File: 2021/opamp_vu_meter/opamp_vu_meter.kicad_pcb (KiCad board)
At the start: 2 copper layers, 80 x 100 mm, 44 parts, among them J1 Conn_01x02, J2 Conn_01x02, Q1 Q_PNP_BCE, U1 TLC272, U2 TLC272, U3 TLC272, U4 TLC272, U5 TLC272

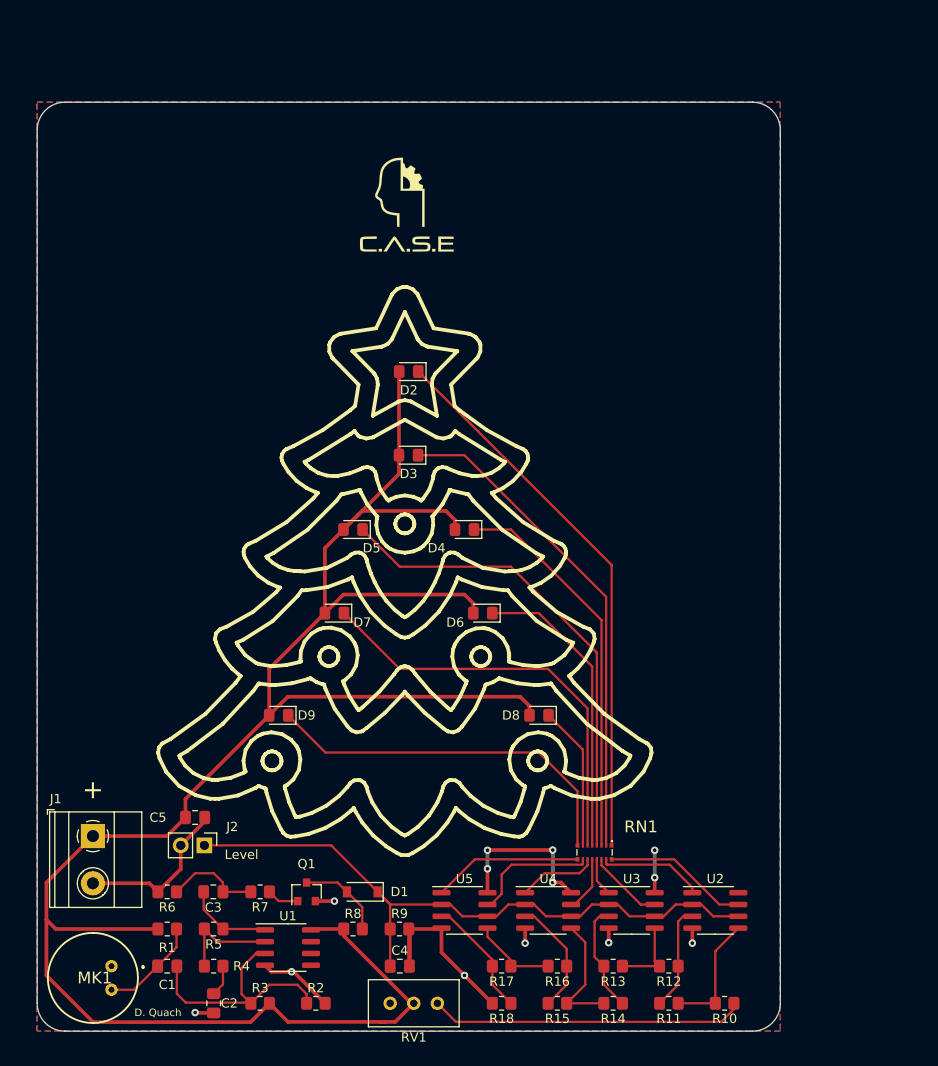
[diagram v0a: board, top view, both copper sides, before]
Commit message: Changed outline shape and component placement
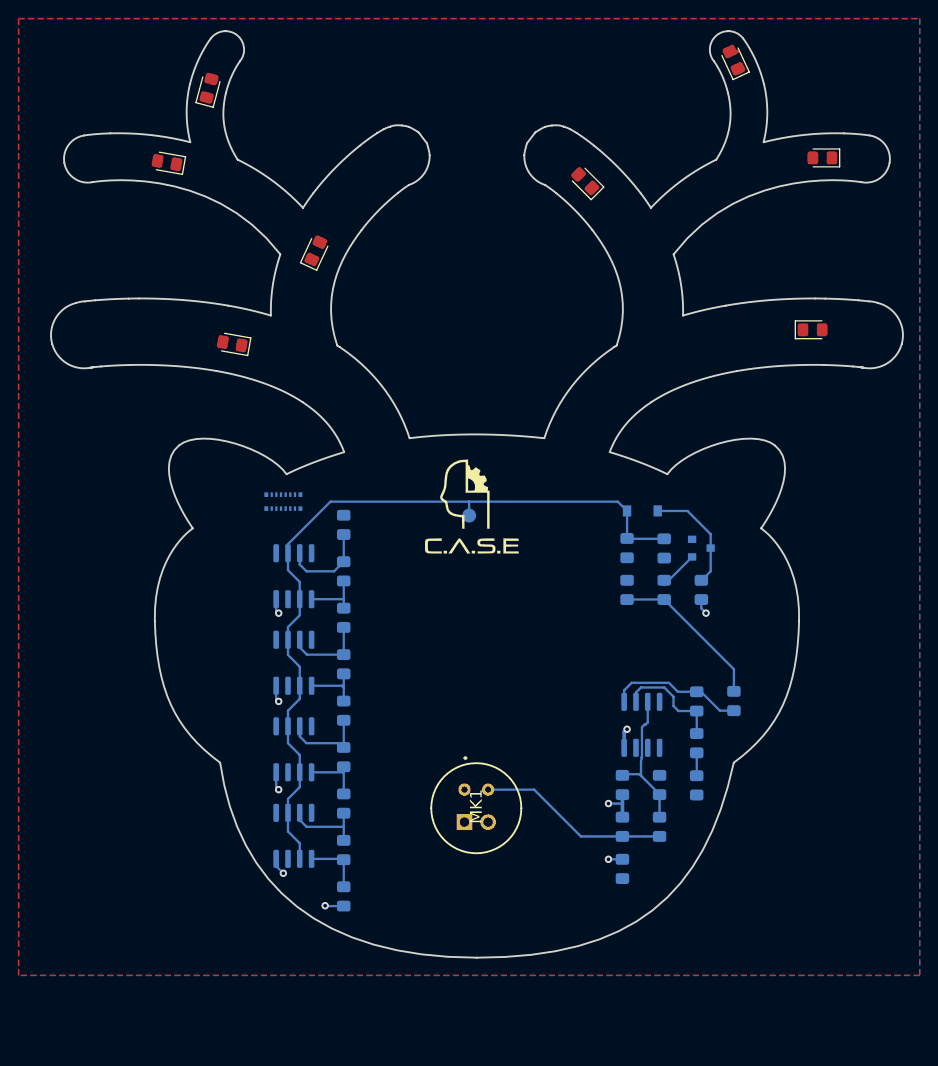
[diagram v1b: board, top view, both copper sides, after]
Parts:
- removed J2: Conn_01x02, Connector_PinHeader_2.54mm:PinHeader_1x02_P2.54mm_Vertical
- removed RV1: R_POT, Potentiometer_THT:Potentiometer_Bourns_3296W_Vertical
- added TP1: TestPoint, TestPoint:TestPoint_Pad_D1.5mm, B.Cu at (149.5, 83.5)
- C1, C2, C3, C4, C5: footprint Capacitor_SMD:C_0805_2012Metric_Pad1.18x1.45mm_HandSolder -> opamp_vu_meter:C_0805_2012Metric_Pad1.18x1.45mm_HandSolder_silkVal; moved to B.Cu
- D1, Q1, RN1, U1, U2, U3, U4, U5: moved to B.Cu
- J1: footprint TerminalBlock_Phoenix:TerminalBlock_Phoenix_MKDS-1,5-2-5.08_1x02_P5.08mm_Horizontal -> Connector_PinHeader_2.54mm:PinHeader_1x02_P2.54mm_Vertical; moved to B.Cu
- R1, R2, R3, R6, R7, R8, R9: footprint Resistor_SMD:R_0805_2012Metric_Pad1.20x1.40mm_HandSolder -> opamp_vu_meter:C_0805_2012Metric_Pad1.18x1.45mm_HandSolder_silkVal; moved to B.Cu
- R10, R18: value R_Small -> 43k; footprint Resistor_SMD:R_0805_2012Metric_Pad1.20x1.40mm_HandSolder -> opamp_vu_meter:C_0805_2012Metric_Pad1.18x1.45mm_HandSolder_silkVal; moved to B.Cu
- R11: value R_Small -> 6.2k; footprint Resistor_SMD:R_0805_2012Metric_Pad1.20x1.40mm_HandSolder -> opamp_vu_meter:C_0805_2012Metric_Pad1.18x1.45mm_HandSolder_silkVal; moved to B.Cu
- R12: value R_Small -> 4.3k; footprint Resistor_SMD:R_0805_2012Metric_Pad1.20x1.40mm_HandSolder -> opamp_vu_meter:C_0805_2012Metric_Pad1.18x1.45mm_HandSolder_silkVal; moved to B.Cu
- R13: value R_Small -> 3k; footprint Resistor_SMD:R_0805_2012Metric_Pad1.20x1.40mm_HandSolder -> opamp_vu_meter:C_0805_2012Metric_Pad1.18x1.45mm_HandSolder_silkVal; moved to B.Cu
- R14: value R_Small -> 2.2k; footprint Resistor_SMD:R_0805_2012Metric_Pad1.20x1.40mm_HandSolder -> opamp_vu_meter:C_0805_2012Metric_Pad1.18x1.45mm_HandSolder_silkVal; moved to B.Cu
- R15: value R_Small -> 1.6k; footprint Resistor_SMD:R_0805_2012Metric_Pad1.20x1.40mm_HandSolder -> opamp_vu_meter:C_0805_2012Metric_Pad1.18x1.45mm_HandSolder_silkVal; moved to B.Cu
- R16: value R_Small -> 1.1k; footprint Resistor_SMD:R_0805_2012Metric_Pad1.20x1.40mm_HandSolder -> opamp_vu_meter:C_0805_2012Metric_Pad1.18x1.45mm_HandSolder_silkVal; moved to B.Cu
- R17: value R_Small -> 750R; footprint Resistor_SMD:R_0805_2012Metric_Pad1.20x1.40mm_HandSolder -> opamp_vu_meter:C_0805_2012Metric_Pad1.18x1.45mm_HandSolder_silkVal; moved to B.Cu
- R4: value 10k -> 1k; footprint Resistor_SMD:R_0805_2012Metric_Pad1.20x1.40mm_HandSolder -> opamp_vu_meter:C_0805_2012Metric_Pad1.18x1.45mm_HandSolder_silkVal; moved to B.Cu
- R5: value 100k -> 200k; footprint Resistor_SMD:R_0805_2012Metric_Pad1.20x1.40mm_HandSolder -> opamp_vu_meter:C_0805_2012Metric_Pad1.18x1.45mm_HandSolder_silkVal; moved to B.Cu
- moved D9 70.9 mm to (186.5, 63.5), turned to 0 degrees
- moved D5 64.4 mm to (187.5, 45.0)
- moved C3 59.7 mm to (178.0, 103.5), turned to 270 degrees
- moved R6 59.2 mm to (166.5, 91.5), turned to 90 degrees
- moved R5 57.5 mm to (174.0, 103.5), turned to 270 degrees
- moved R4 57.3 mm to (174.0, 108.0), turned to 270 degrees
- moved C2 57.0 mm to (174.0, 112.5)
- moved Q1 56.3 mm to (174.5, 87.0), turned to 0 degrees
- moved C1 55.1 mm to (170.0, 117.0), turned to 90 degrees
- moved R7 54.3 mm to (170.5, 91.5), turned to 270 degrees
- moved R18 54.2 mm to (136.0, 84.5), turned to 90 degrees
- moved D7 53.8 mm to (162.0, 47.5), turned to 135 degrees
- moved C4 53.2 mm to (170.5, 87.0), turned to 270 degrees
- moved R8 52.3 mm to (174.5, 91.5), turned to 90 degrees
- moved D8 51.9 mm to (124.0, 65.0), turned to 170 degrees
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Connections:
- J1 pad 1: VCC -> GND
- J1 pad 2: GND -> VCC
- R10 pad 1: Net-(R10-Pad1) -> VCC
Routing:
- net VCC: track 242.2 -> 19.3 mm, vias 6 -> 9
- net Net-(D2-Pad1): track 59.6 -> 0.00 mm
- net Net-(D3-Pad1): track 53.3 -> 0.00 mm
- net GND: track 52.5 -> 0.00 mm, vias 7 -> 0
- net Net-(D5-Pad1): track 51.5 -> 0.00 mm
- net Net-(D7-Pad1): track 45.2 -> 0.00 mm
- net Net-(D4-Pad1): track 42.0 -> 0.00 mm
- net Net-(D9-Pad1): track 40.4 -> 0.00 mm
- net Net-(R10-Pad1): track 33.8 -> 0.00 mm
- net Net-(D6-Pad1): track 32.4 -> 0.00 mm
- net Net-(RN1-Pad9): track 16.1 -> 0.00 mm
- net Net-(RN1-Pad10): track 15.7 -> 0.00 mm
- net Net-(D8-Pad1): track 15.5 -> 0.00 mm
- net Net-(RN1-Pad11): track 13.8 -> 0.00 mm
- net AudioLevel: track 72.4 -> 84.8 mm
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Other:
- board size 80 x 100 mm -> 91.7 x 99.7 mm
- board text added: "AMPLIFIER"
- board text added: "Audio Level"
- board text added: "BATTERY"
- board text added: "JLCJLCJLCJLC"
- board text added: "LOGARITHMIC ADC + LED DRIVER"
- board text added: "PEAK DETECTOR"
- board text removed: "+"
- board text removed: "Level"

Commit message: Final version (hopefully)
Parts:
- removed R10: 43k, opamp_vu_meter:C_0805_2012Metric_Pad1.18x1.45mm_HandSolder_silkVal
- removed TP1: TestPoint, TestPoint:TestPoint_Pad_D1.5mm
- added Audiolevel_TP1: TestPoint, TestPoint:TestPoint_Pad_D1.5mm, B.Cu at (150.0, 89.5)
- added G***: LOGO, print:godjul, F.Cu at (151.0, 78.8)
- added G***: LOGO, print:eyes, F.Cu at (150.5, 101.0)
- added REF**: MountingHole_3.2mm_M3, MountingHole:MountingHole_3.2mm_M3, F.Cu at (122.5, 80.0)
- added REF**: MountingHole_3.2mm_M3, MountingHole:MountingHole_3.2mm_M3, F.Cu at (178.5, 80.0)
- added RN2: R_Pack04, opamp_vu_meter:R_Array_Convex_4x1206_long, B.Cu at (125.0, 94.7)
- added RV1: R_POT, Potentiometer_SMD:Potentiometer_Bourns_TC33X_Vertical, B.Cu at (134.0, 124.0)
- C4: value C_Small -> 220nF
- R5: value 200k -> 100k
- R9: value R_Small -> 220K
- RN1: value EXB-2HV331JV -> R_Pack04; footprint SamacSys_Parts:EXB2HV331JV -> opamp_vu_meter:R_Array_Convex_4x1206_long
- moved RN1 22.7 mm to (125.0, 104.2), turned to 90 degrees
- moved D8 12.8 mm to (111.2, 64.1), turned to 180 degrees
- moved D6 8.59 mm to (138.0, 48.0), turned to 45 degrees
- moved D7 7.65 mm to (166.8, 53.5), turned to 120 degrees
- moved D9 7.23 mm to (179.3, 64.2), turned to 5 degrees
- moved D5 6.10 mm to (181.5, 46.2), turned to 10 degrees
- moved G*** 4.28 mm to (149.5, 86.8)
- moved D3 2.93 mm to (122.5, 34.8), turned to 70 degrees
- moved D2 2.82 mm to (179.2, 37.0), turned to 105 degrees
- moved D4 1.99 mm to (115.0, 45.2), turned to 175 degrees
- moved R11 0.50 mm to (136.5, 119.5)
- moved R12 0.50 mm to (136.5, 114.5)
- moved R13 0.50 mm to (136.5, 109.5)
- moved R14 0.50 mm to (136.5, 104.5)
- moved R15 0.50 mm to (136.5, 99.5)
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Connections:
- RN1 pad 1: Net-(D2-Pad1) -> Net-(RN1-Pad1)
- RN1 pad 2: Net-(D3-Pad1) -> Net-(RN1-Pad2)
- RN1 pad 3: Net-(D4-Pad1) -> Net-(RN1-Pad3)
- RN1 pad 4: Net-(D5-Pad1) -> Net-(RN1-Pad4)
- RN1 pad 5: Net-(D6-Pad1) -> Net-(D5-Pad1)
- RN1 pad 6: Net-(D7-Pad1) -> Net-(D4-Pad1)
- RN1 pad 7: Net-(D8-Pad1) -> Net-(D3-Pad1)
- RN1 pad 8: Net-(D9-Pad1) -> Net-(D2-Pad1)
- U2 pad 1: Net-(RN1-Pad16) -> Net-(RN1-Pad2)
- U2 pad 7: Net-(RN1-Pad10) -> Net-(RN1-Pad1)
- U3 pad 1: Net-(RN1-Pad14) -> Net-(RN1-Pad4)
- U3 pad 7: Net-(RN1-Pad15) -> Net-(RN1-Pad3)
- U4 pad 1: Net-(RN1-Pad12) -> Net-(RN2-Pad2)
- U4 pad 7: Net-(RN1-Pad13) -> Net-(RN2-Pad1)
- U5 pad 1: Net-(RN1-Pad9) -> Net-(RN2-Pad4)
- U5 pad 7: Net-(RN1-Pad11) -> Net-(RN2-Pad3)
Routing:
- net Net-(D2-Pad1): track 0.00 -> 108.6 mm, vias 0 -> 1
- net Net-(D5-Pad1): track 0.00 -> 103.1 mm, vias 0 -> 1
- net Net-(D3-Pad1): track 0.00 -> 85.7 mm, vias 0 -> 1
- net Net-(D4-Pad1): track 0.00 -> 80.6 mm, vias 0 -> 1
- net Net-(D7-Pad1): track 0.00 -> 72.5 mm, vias 0 -> 1
- net Net-(D9-Pad1): track 0.00 -> 72.2 mm, vias 0 -> 1
- net Net-(D6-Pad1): track 0.00 -> 60.2 mm, vias 0 -> 1
- net Net-(D8-Pad1): track 0.00 -> 59.0 mm, vias 0 -> 1
- net Net-(RN1-Pad1): track 0.00 -> 15.9 mm
- net Net-(RN2-Pad4): track 0.00 -> 13.4 mm
- net Net-(RN1-Pad3): track 0.00 -> 12.2 mm
- net Net-(RN1-Pad2): track 0.00 -> 11.0 mm
- net Net-(RN1-Pad4): track 0.00 -> 10.4 mm
- net Net-(RN2-Pad3): track 0.00 -> 9.03 mm
- net Net-(RN2-Pad1): track 0.00 -> 6.77 mm
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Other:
- board text added: "A. Anderson"
- board text added: "CASE julkort 2021"
- board text added: "LOGARITHMIC COMPARATORS"
- board text removed: "Audio Level"
- board text removed: "LOGARITHMIC ADC + LED DRIVER"

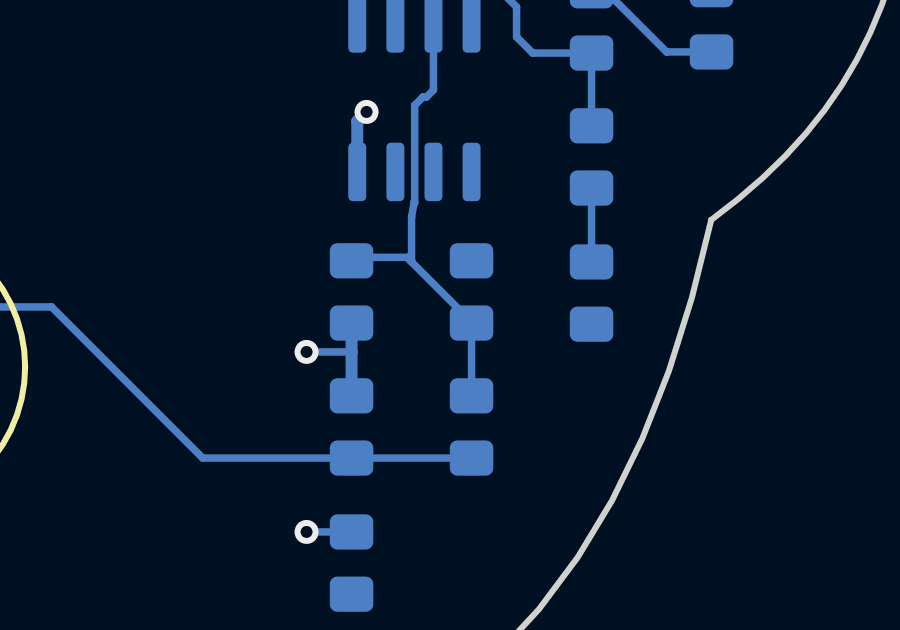
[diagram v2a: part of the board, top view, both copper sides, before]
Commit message: Minor revision with zener to stabilize
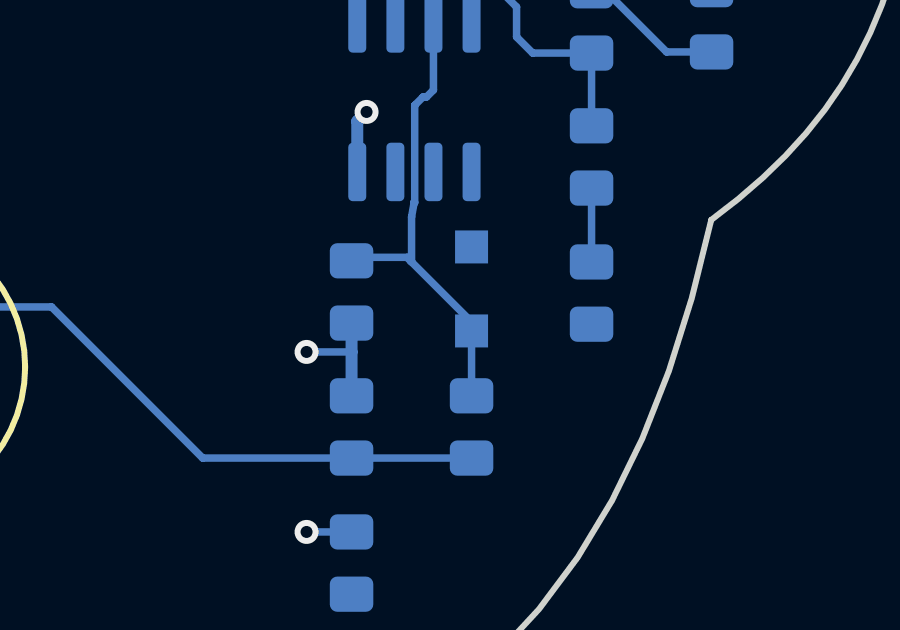
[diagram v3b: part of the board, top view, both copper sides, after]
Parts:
- removed R2: 100k, opamp_vu_meter:C_0805_2012Metric_Pad1.18x1.45mm_HandSolder_silkVal
- added Z1: MM3Z4V3, Diode_SMD:D_SOD-123F, B.Cu at (170.0, 112.4)
- C5: value 1uF -> 10uF
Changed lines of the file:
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@@
       (psa4output false)
       (plotreference true)
-      (plotvalue false)
+      (plotvalue true)
       (plotinvisibletext false)
       (padsonsilk false)
@@
       (effects (font (size 1 1) (thickness 0.15)))
     )
-    (fp_text user %R (at 0.3 0) (layer F.Fab)
-      (effects (font (size 1 1) (thickness 0.15)))
-    )
     (fp_circle (center 0 0) (end 3.2 0) (layer Cmts.User) (width 0.15))
     (fp_circle (center 0 0) (end 3.45 0) (layer F.CrtYd) (width 0.05))
+    (fp_text user %R (at 0.3 0) (layer F.Fab)
+      (effects (font (size 1 1) (thickness 0.15)))
+    )
     (pad 1 np_thru_hole circle (at 0 0) (size 3.2 3.2) (drill 3.2) (layers *.Cu *.Mask))
   )
@@
       (effects (font (size 1 1) (thickness 0.15)))
     )
-    (fp_text value 1uF (at -0.0375 -1.5 90) (layer B.SilkS)
+    (fp_text value 10uF (at -0.0375 -1.5 90) (layer B.SilkS)
       (effects (font (size 1 1) (thickness 0.15)) (justify mirror))
     )
@@
     (pad 1 smd roundrect (at -1.0375 0 90) (size 1.175 1.45) (layers B.Cu B.Paste B.Mask) (roundrect_rratio 0.2127659574468085)
       (net 26 "Net-(R17-Pad2)"))
-    (model ${KISYS3DMOD}/Capacitor_SMD.3dshapes/C_0805_2012Metric.wrl
-      (at (xyz 0 0 0))
-      (scale (xyz 1 1 1))
-      (rotate (xyz 0 0 0))
-    )
-  )
-  (module opamp_vu_meter:C_0805_2012Metric_Pad1.18x1.45mm_HandSolder_silkVal (layer B.Cu)
-    (at 170 112.5 90)
-    (descr "Capacitor SMD 0805 (2012 Metric), square (rectangular) end terminal, IPC_7351 nominal with elongated pad for handsoldering. (Body size source: IPC-SM-782 page 76, https://www.pcb-3d.com/wordpress/wp-content/uploads/ipc-sm-782a_amendment_1_and_2.pdf, https://docs.google.com/spreadsheets/d/1BsfQQcO9C6DZCsRaXUlFlo91Tg2WpOkGARC1WS5S8t0/edit?usp=sharing), generated with kicad-footprint-generator")
-    (tags "capacitor handsolder")
-    (attr smd)
-    (fp_text reference R2 (at -0.0375 -1.5 90) (layer F.Fab) hide
-      (effects (font (size 1 1) (thickness 0.15)))
-    )
-    (fp_text value 100k (at 0 -1.5 90) (layer B.SilkS)
-      (effects (font (size 1 1) (thickness 0.15)) (justify mirror))
-    )
-    (fp_line (start 1.88 -0.98) (end -1.88 -0.98) (layer B.CrtYd) (width 0.05))
-    (fp_line (start 1.88 0.98) (end 1.88 -0.98) (layer B.CrtYd) (width 0.05))
-    (fp_line (start -1.88 0.98) (end 1.88 0.98) (layer B.CrtYd) (width 0.05))
-    (fp_line (start -1.88 -0.98) (end -1.88 0.98) (layer B.CrtYd) (width 0.05))
-    (fp_line (start -0.261252 -0.735) (end 0.261252 -0.735) (layer B.SilkS) (width 0.12))
-    (fp_line (start -0.261252 0.735) (end 0.261252 0.735) (layer B.SilkS) (width 0.12))
-    (fp_line (start 1 -0.625) (end -1 -0.625) (layer B.Fab) (width 0.1))
-    (fp_line (start 1 0.625) (end 1 -0.625) (layer B.Fab) (width 0.1))
-    (fp_line (start -1 0.625) (end 1 0.625) (layer B.Fab) (width 0.1))
-    (fp_line (start -1 -0.625) (end -1 0.625) (layer B.Fab) (width 0.1))
-    (fp_text user %R (at -0.0375 0 90) (layer B.Fab)
-      (effects (font (size 0.5 0.5) (thickness 0.08)) (justify mirror))
-    )
-    (pad 2 smd roundrect (at 1.0375 0 90) (size 1.175 1.45) (layers B.Cu B.Paste B.Mask) (roundrect_rratio 0.2127659574468085)
-      (net 4 GND))
-    (pad 1 smd roundrect (at -1.0375 0 90) (size 1.175 1.45) (layers B.Cu B.Paste B.Mask) (roundrect_rratio 0.2127659574468085)
-      (net 1 "Net-(C1-Pad2)"))
     (model ${KISYS3DMOD}/Capacitor_SMD.3dshapes/C_0805_2012Metric.wrl
       (at (xyz 0 0 0))
@@
     (pad 1 smd circle (at 0 0) (size 1.5 1.5) (layers B.Cu B.Mask)
       (net 7 AudioLevel))
+  )
+  (module Diode_SMD:D_SOD-123F (layer B.Cu)
+    (at 170 112.4 270)
+    (descr D_SOD-123F)
+    (tags D_SOD-123F)
+    (attr smd)
+    (fp_text reference Z1 (at -0.127 -2 270) (layer B.SilkS)
+      (effects (font (size 1 1) (thickness 0.15)) (justify mirror))
+    )
+    (fp_text value MM3Z4V3 (at 0 -2.1 270) (layer B.Fab)
+      (effects (font (size 1 1) (thickness 0.15)) (justify mirror))
+    )
+    (fp_line (start -2.2 1) (end 1.65 1) (layer B.SilkS) (width 0.12))
+    (fp_line (start -2.2 -1) (end 1.65 -1) (layer B.SilkS) (width 0.12))
+    (fp_line (start -2.2 1.15) (end -2.2 -1.15) (layer B.CrtYd) (width 0.05))
+    (fp_line (start 2.2 -1.15) (end -2.2 -1.15) (layer B.CrtYd) (width 0.05))
+    (fp_line (start 2.2 1.15) (end 2.2 -1.15) (layer B.CrtYd) (width 0.05))
+    (fp_line (start -2.2 1.15) (end 2.2 1.15) (layer B.CrtYd) (width 0.05))
+    (fp_line (start -1.4 0.9) (end 1.4 0.9) (layer B.Fab) (width 0.1))
+    (fp_line (start 1.4 0.9) (end 1.4 -0.9) (layer B.Fab) (width 0.1))
+    (fp_line (start 1.4 -0.9) (end -1.4 -0.9) (layer B.Fab) (width 0.1))
+    (fp_line (start -1.4 -0.9) (end -1.4 0.9) (layer B.Fab) (width 0.1))
+    (fp_line (start -0.75 0) (end -0.35 0) (layer B.Fab) (width 0.1))
+    (fp_line (start -0.35 0) (end -0.35 0.55) (layer B.Fab) (width 0.1))
+    (fp_line (start -0.35 0) (end -0.35 -0.55) (layer B.Fab) (width 0.1))
+    (fp_line (start -0.35 0) (end 0.25 0.4) (layer B.Fab) (width 0.1))
+    (fp_line (start 0.25 0.4) (end 0.25 -0.4) (layer B.Fab) (width 0.1))
+    (fp_line (start 0.25 -0.4) (end -0.35 0) (layer B.Fab) (width 0.1))
+    (fp_line (start 0.25 0) (end 0.75 0) (layer B.Fab) (width 0.1))
+    (fp_line (start -2.2 1) (end -2.2 -1) (layer B.SilkS) (width 0.12))
+    (fp_text user %R (at -0.127 1.905 270) (layer B.Fab)
+      (effects (font (size 1 1) (thickness 0.15)) (justify mirror))
+    )
+    (pad 1 smd rect (at -1.4 0 270) (size 1.1 1.1) (layers B.Cu B.Paste B.Mask)
+      (net 4 GND))
+    (pad 2 smd rect (at 1.4 0 270) (size 1.1 1.1) (layers B.Cu B.Paste B.Mask)
+      (net 1 "Net-(C1-Pad2)"))
+    (model ${KISYS3DMOD}/Diode_SMD.3dshapes/D_SOD-123F.wrl
+      (at (xyz 0 0 0))
+      (scale (xyz 1 1 1))
+      (rotate (xyz 0 0 0))
+    )
   )
   (gr_text "CASE julkort 2021" (at 188 45) (layer B.SilkS)
@@
     (effects (font (size 0.8 0.8) (thickness 0.15)) (justify mirror))
   )
-  (segment (start 170 115.9625) (end 170 113.5375) (width 0.25) (layer B.Cu) (net 1))
-  (segment (start 170 113.5375) (end 170 113.5) (width 0.25) (layer B.Cu) (net 1))
-  (segment (start 170 113.5) (end 167.9625 111.4625) (width 0.25) (layer B.Cu) (net 1))
   (segment (start 167.9625 111.4625) (end 167.846376 111.346376) (width 0.25) (layer B.Cu) (net 1))
   (segment (start 167.846376 111.346376) (end 166.116124 111.346376) (width 0.25) (layer B.Cu) (net 1))
@@
   (segment (start 168.08501 109.501778) (end 168.10499 109.521758) (width 0.25) (layer B.Cu) (net 1))
   (segment (start 168.08501 109.521758) (end 168.08501 109.501778) (width 0.25) (layer B.Cu) (net 1))
+  (segment (start 170 113.5) (end 170 113.8) (width 0.25) (layer B.Cu) (net 1))
+  (segment (start 167.9625 111.4625) (end 170 113.5) (width 0.25) (layer B.Cu) (net 1))
+  (segment (start 170 115.9625) (end 170 113.8) (width 0.25) (layer B.Cu) (net 1))
   (segment (start 166 118.0375) (end 170 118.0375) (width 0.25) (layer B.Cu) (net 2))
   (segment (start 161.0375 118.0375) (end 166 118.0375) (width 0.25) (layer B.Cu) (net 2))

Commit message: Rotate one component
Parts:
- turned Z1 to 90 degrees
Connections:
- Z1 pad 1: GND -> Net-(C1-Pad2)
- Z1 pad 2: Net-(C1-Pad2) -> GND

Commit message: Updated peak detector values
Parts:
- C4: value 220nF -> 100n
- R9: value 220K -> 10M
